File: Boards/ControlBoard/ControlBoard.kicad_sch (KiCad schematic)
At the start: 13 parts, among them J1 TBP02R2W-381-06BE, J11 Conn_02x10_Counter_Clockwise, J12 Conn_02x10_Counter_Clockwise, J13 Conn_02x10_Counter_Clockwise, J14 Conn_02x10_Counter_Clockwise, J2 TBP02R2W-381-06BE, J23 776231-1, J3 TBP01R2W-508-02BE, J4 TBP01R1-508-04BE, J5 Conn_02x10_Counter_Clockwise, J7 TBP02R2W-381-08BE, J8 TBP02R2W-381-08BE

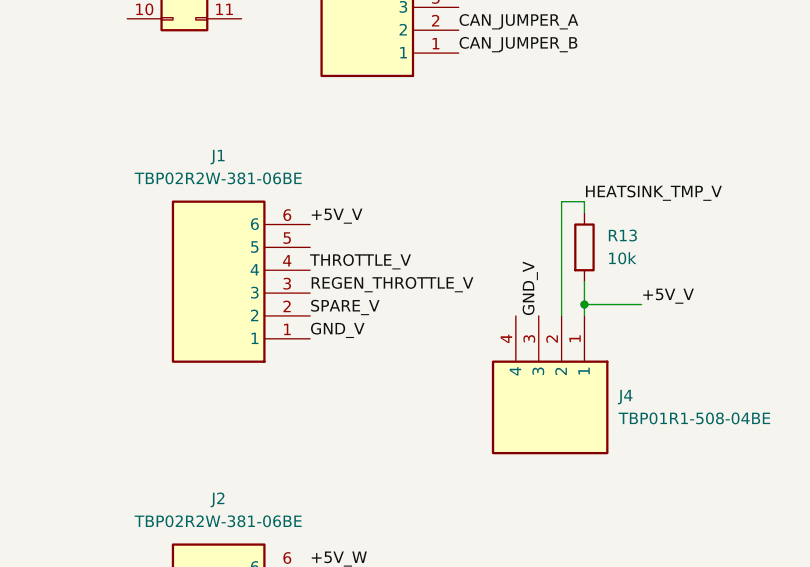
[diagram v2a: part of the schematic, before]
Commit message: Layout controlboard, update cad
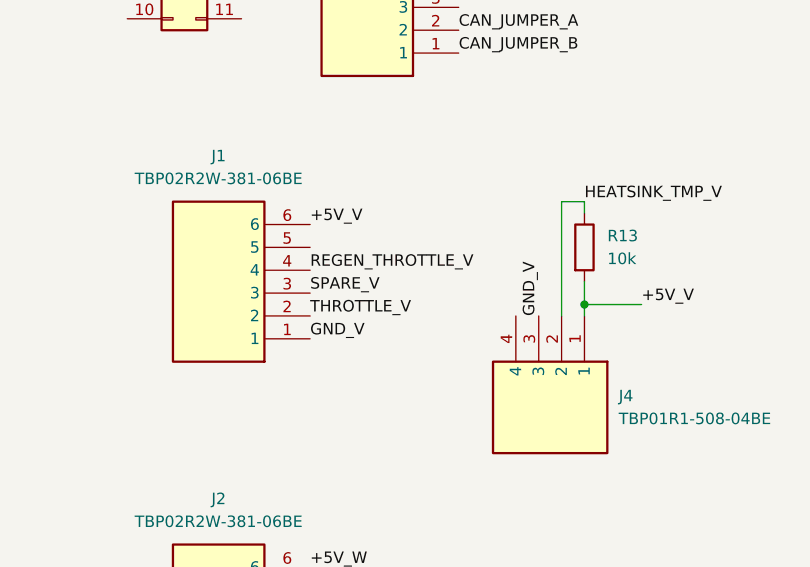
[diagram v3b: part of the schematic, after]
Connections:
- net REGEN_THROTTLE_V: now also J1.4; no longer J1.3
- net SPARE_V: now also J1.3; no longer J1.2
- net THROTTLE_V: now also J1.2; no longer J1.4
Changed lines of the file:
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@@
+		)
+	)
+	(label "THROTTLE_V"
+		(at 40.64 71.12 0)
+		(effects
+			(font
+				(size 1.27 1.27)
+			)
+			(justify left bottom)
 		)
 	)
@@
 		)
 	)
-	(label "THROTTLE_V"
-		(at 40.64 66.04 0)
-		(effects
-			(font
-				(size 1.27 1.27)
-			)
-			(justify left bottom)
-		)
-	)
 	(label "SPI2_ADC4_CS_A"
 		(at 152.4 50.8 0)
@@
 		)
 	)
-	(label "SPARE_V"
-		(at 40.64 71.12 0)
-		(effects
-			(font
-				(size 1.27 1.27)
-			)
-			(justify left bottom)
-		)
-	)
 	(label "SPI2_SCK_A"
 		(at 152.4 55.88 0)
@@
 		)
 	)
-	(label "REGEN_THROTTLE_V"
-		(at 40.64 68.58 0)
-		(effects
-			(font
-				(size 1.27 1.27)
-			)
-			(justify left bottom)
-		)
-	)
 	(label "HALL_PH_V_W"
 		(at 114.3 64.77 180)
@@
 		)
 	)
+	(label "SPARE_V"
+		(at 40.64 68.58 0)
+		(effects
+			(font
+				(size 1.27 1.27)
+			)
+			(justify left bottom)
+		)
+	)
 	(label "THROTTLE_V"
 		(at 114.3 49.53 180)
@@
 		)
 	)
+	(label "REGEN_THROTTLE_V"
+		(at 40.64 66.04 0)
+		(effects
+			(font
+				(size 1.27 1.27)
+			)
+			(justify left bottom)
+		)
+	)

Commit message: fix connector pinout
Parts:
- removed J23: 776231-1, InverterCom:7762311, symbol InverterCom:776231-1
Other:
- note removed: "THE FOLLOWING PINOUT IS BASED ON SEVCON GEN 4 INVERTERS, AND IS INTENDED TO BE A PIN-COMPATIBLE REPLACEMENT (PLEASE REFERENCE: https://www.thunderstruck-ev.com/images/Gen4%20Product%20Manual%20V3%204.pdf)"
- note removed: "TODO: CONNECTOR FOR ADC INPUTS (THROTTLE/ENCODER/TMP) - INTERNAL CONN FOR VOLTAGE/CURRENT SENSE INPUTS - DIGITAL INPUT (MAYBE TWO), DRIVE INTERLOCK (TURNS OFF RELAY OR SMTH TO DISCONN POWER) - RELAY OUTPUT CONNECTOR - WIRING HARNESS ADAPTER FROM OUR CONNECTORS TO ZERO'S 35 PIN."
- note removed: "TODO: connect reset/fault lines, also layout connectors, etc."
- note removed: "ZERO COMPATIBILITY REQUIREMENTS - KEY INPUT (LIVE TO BATTERY RELATIVE TO BATT- ON 6/1) - NEEDS TO SUPPORT SEVCON CANBUS TERM JUMPER - NEEDS 24V PSU (CANBUS) OUT ON 28 - NEEDS CAN LOW/HIGH (27/16) - NEEDS DIGITAL INPUT ON 18 - ENCODER POWER GND ON 15 - ENCODER POWER + (5V) ON 26 - COSINE INPUT ON 35 - MOTOR TEMP SENSE ON 33 (EXPECTING IT TO BE TIED TO INV-COM) - THROTTLE IDLE SWITCH ON 30 - THROTT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"
- moved on the sheet: J11, J12, J14, J5, J7, J8
